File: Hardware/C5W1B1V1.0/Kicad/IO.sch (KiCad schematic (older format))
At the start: 3 parts, among them J1 Conn_02x20_Counter_Clockwise, J2 Conn_02x20_Counter_Clockwise, J4 Conn_01x04

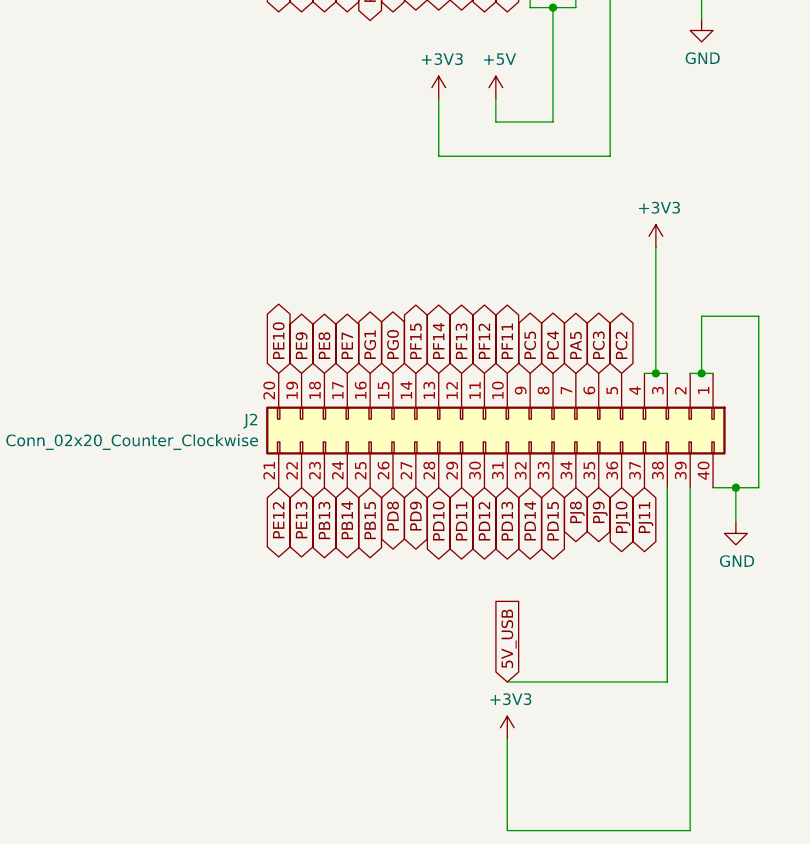
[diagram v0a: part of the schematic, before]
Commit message: Dodano mikrofony i więcej WS2812B
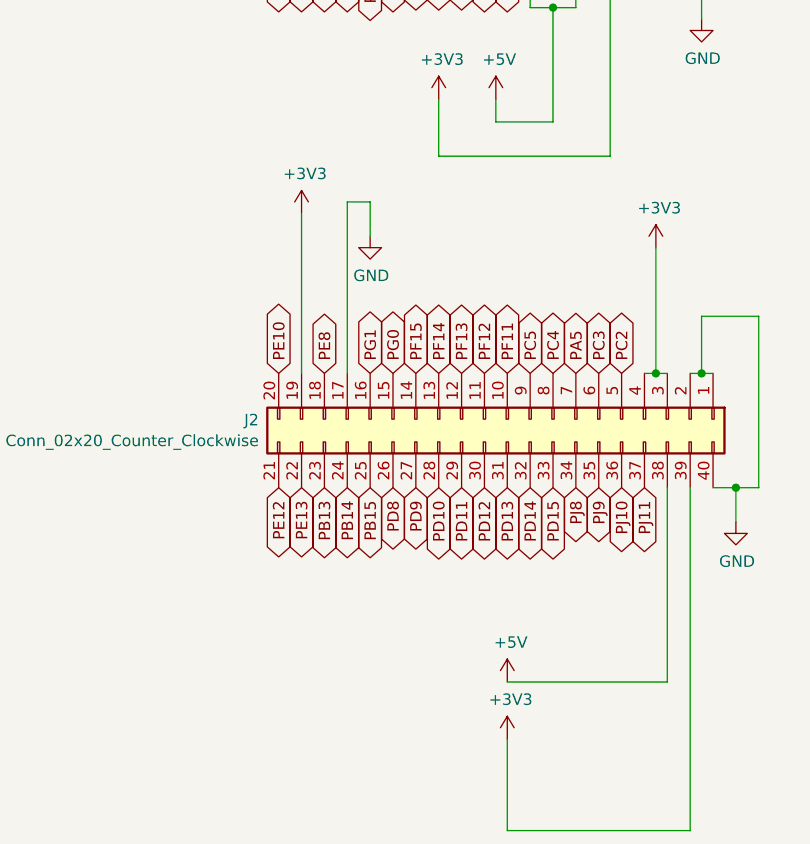
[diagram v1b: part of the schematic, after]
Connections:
- net 5V_USB is gone; now on net +5V: J2.38 (Pin_38)
- net PE7 is gone; now on net GND: J2.17 (Pin_17)
- net PE9 is gone; now on net +3V3: J2.19 (Pin_19)
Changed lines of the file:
@@
 $Descr A4 11693 8268
 encoding utf-8
-Sheet 3 8
+Sheet 3 9
 Title ""
 Date ""
@@
 Text GLabel 3000 5050 1    50   BiDi ~ 0
 PG0
-Text GLabel 2600 5050 1    50   BiDi ~ 0
-PE9
 Text GLabel 2700 5050 1    50   BiDi ~ 0
 PE8
-Text GLabel 2800 5050 1    50   BiDi ~ 0
-PE7
 Text GLabel 2900 5050 1    50   BiDi ~ 0
 PG1
@@
 Wire Wire Line
 	3450 3950 3450 3850
-Text GLabel 3500 6400 1    50   Input ~ 0
-5V_USB
 $Comp
 L power:+5V #PWR0173
@@
 	1    0    0    -1
 $EndComp
+Wire Wire Line
+	2600 5050 2600 4350
+$Comp
+L power:+3V3 #PWR0264
+U 1 1 6748E99D
+P 2600 4350
+F 0 "#PWR0264" H 2600 4200 50  0001 C CNN
+F 1 "+3V3" H 2615 4523 50  0000 C CNN
+F 2 "" H 2600 4350 50  0001 C CNN
+F 3 "" H 2600 4350 50  0001 C CNN
+	1    2600 4350
+	1    0    0    -1
+$EndComp
+Wire Wire Line
+	2800 5050 2800 4300
+Wire Wire Line
+	2800 4300 2900 4300
+Wire Wire Line
+	2900 4300 2900 4450
+$Comp
+L power:GND #PWR0265
+U 1 1 6749062B
+P 2900 4450
+F 0 "#PWR0265" H 2900 4200 50  0001 C CNN
+F 1 "GND" H 2905 4277 50  0000 C CNN
+F 2 "" H 2900 4450 50  0001 C CNN
+F 3 "" H 2900 4450 50  0001 C CNN
+	1    2900 4450
+	1    0    0    -1
+$EndComp
+$Comp
+L power:+5V #PWR?
+U 1 1 676048BF
+P 3500 6400
+F 0 "#PWR?" H 3500 6250 50  0001 C CNN
+F 1 "+5V" H 3515 6573 50  0000 C CNN
+F 2 "" H 3500 6400 50  0001 C CNN
+F 3 "" H 3500 6400 50  0001 C CNN
+	1    3500 6400
+	1    0    0    -1
+$EndComp
